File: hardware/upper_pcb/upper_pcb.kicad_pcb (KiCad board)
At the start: 2 copper layers, 54 x 54 mm, 12 parts, among them J5 FPC_6pin_0.5mm, SW4 Kailh_GM_8.0, SW5 Kailh_GM_8.0, SW6 Kailh_BlueDot_Side, SW7 Kailh_BlueDot_Side

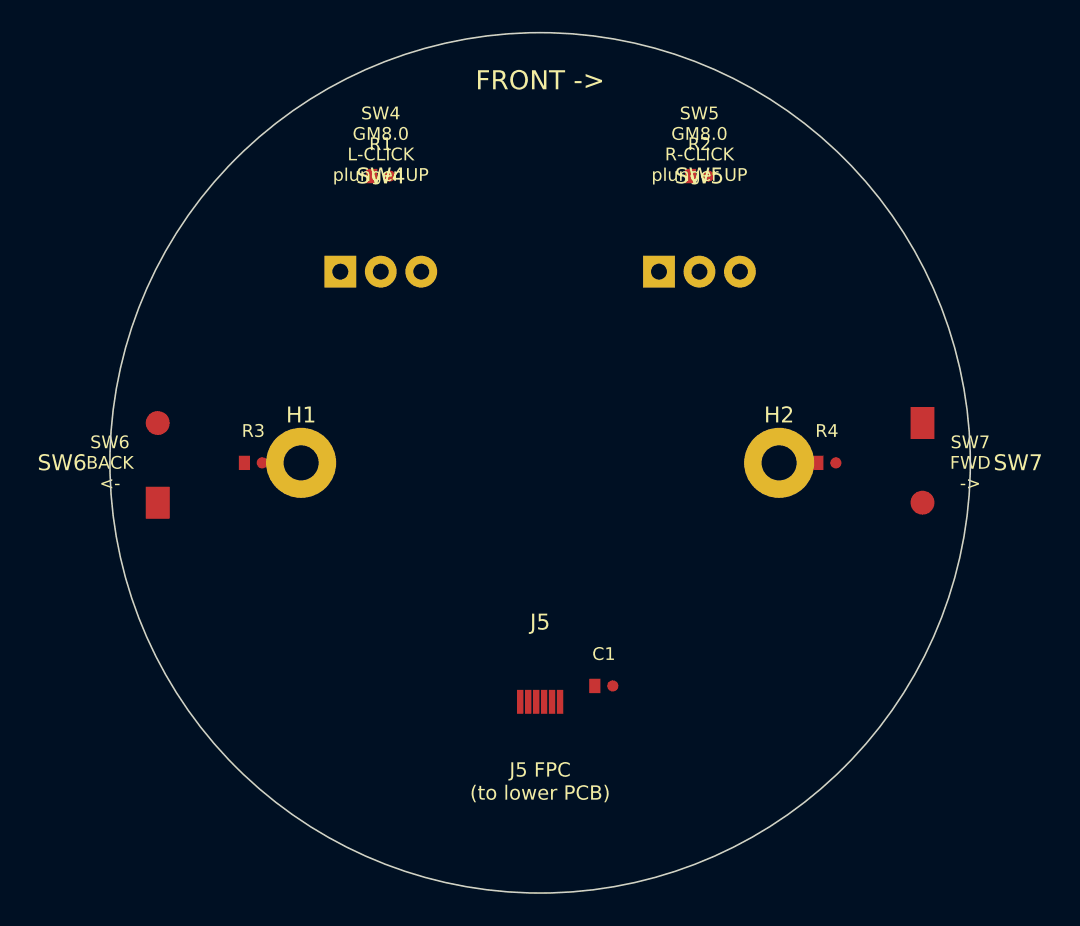
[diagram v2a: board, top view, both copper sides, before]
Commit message: feat: KiCad PCB files with full netlist and copper traces
lower_pcb.kicad_pcb (rev 2.4):
- All pads with correct net assignments
- 91 trace segments/vias covering all nets:
  3V3 rail, GND pour taps, VBUS, BAT_PLUS, SW_OUT (LDO)
  JOY_X/Y/SW from XIAO to Alps RKJXV pads
  BTN_L/R/BK/FW from XIAO to FPC J3 pins
  BT_SYNC from XIAO to SW_BT + R_PU_BT
  BAT_PLUS on B.Cu from J2 to SW1
- Via to B.Cu for J2 battery connector routing

upper_pcb.kicad_pcb (rev 1.6):
- All pads: SW4/SW5 GM8.0 THT, SW6/SW7 Blue Dot SMD, R1-R4, C1, J5 FPC on B.Cu
- 52 trace segments/vias:
  3V3 rail via from J5 B.Cu through to F.Cu R1-R4 pull-ups
  GND rail to all switch COM/GND pads and C1
  BTN_L/R via FPC->pull-up->switch signal pad for all 4 buttons

Open in KiCad 7, run DRC, fix any remaining unrouted connections with interactive router
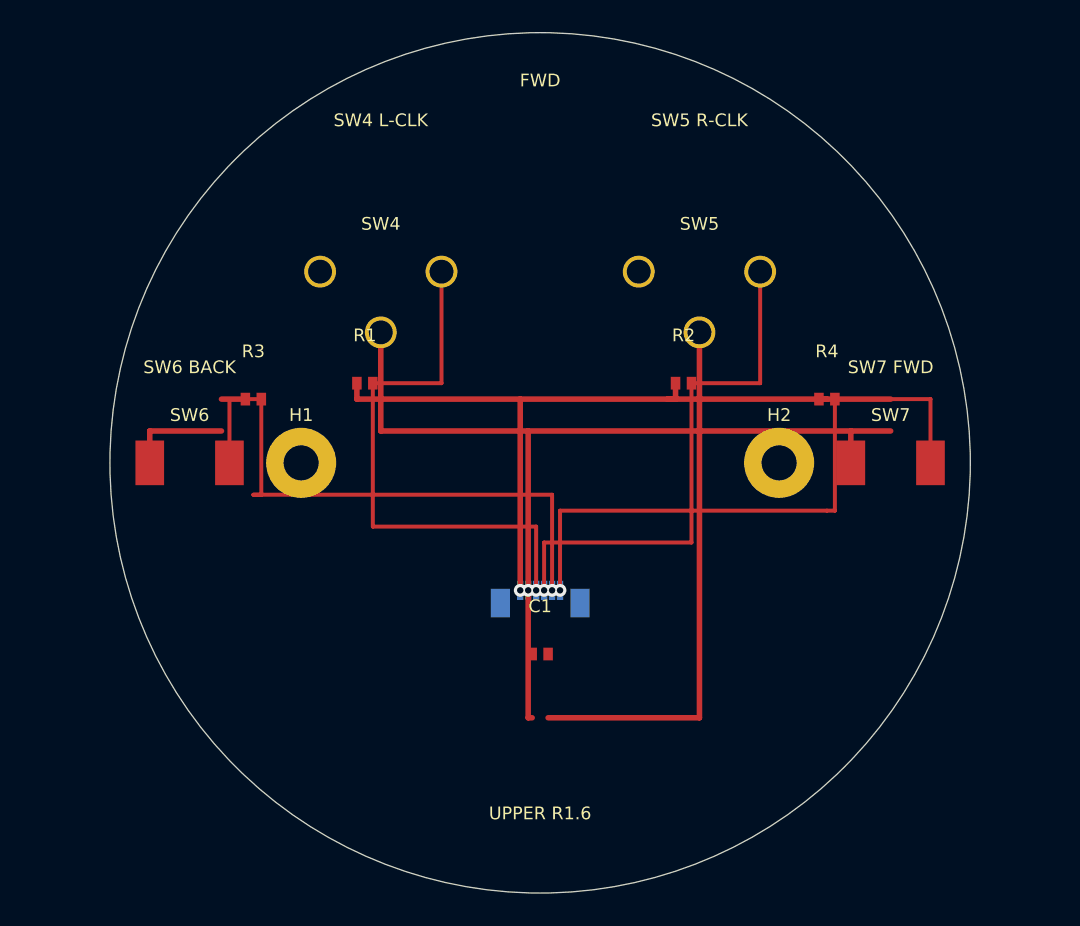
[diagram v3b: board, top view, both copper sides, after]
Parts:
- C1: value 100nF -> C-0402; footprint Capacitor_SMD:C_0402_1005Metric -> C1
- H1: value MountingHole_M2 -> M2-Mount; footprint MountingHole:MountingHole_2.2mm_M2_Pad -> H1
- H2: value MountingHole_M2 -> M2-Mount; footprint MountingHole:MountingHole_2.2mm_M2_Pad -> H2
- J5: value FPC_6pin_0.5mm -> FPC-6P-0.5mm; footprint Connector_FFC-FPC:Hirose_FH12-6S-0.5SH_1x06-1MP_P0.5mm_Horizontal -> J5; moved to B.Cu
- R1: value 10k -> R-0402; footprint Resistor_SMD:R_0402_1005Metric -> R1
- R2: value 10k -> R-0402; footprint Resistor_SMD:R_0402_1005Metric -> R2
- R3: value 10k -> R-0402; footprint Resistor_SMD:R_0402_1005Metric -> R3
- R4: value 10k -> R-0402; footprint Resistor_SMD:R_0402_1005Metric -> R4
- SW4: value Kailh_GM_8.0 -> Kailh-GM8.0; footprint Button_Switch_THT:SW_Push_SPDT_CherryMX_12.8x5.8mm -> SW4
- SW5: value Kailh_GM_8.0 -> Kailh-GM8.0; footprint Button_Switch_THT:SW_Push_SPDT_CherryMX_12.8x5.8mm -> SW5
- SW6: value Kailh_BlueDot_Side -> Kailh-BlueDot; footprint Button_Switch_SMD:SW_Push_Side_8.75mm -> SW6
- SW7: value Kailh_BlueDot_Side -> Kailh-BlueDot; footprint Button_Switch_SMD:SW_Push_Side_8.75mm -> SW7
- moved R1 13.0 mm to (89.0, 95.0)
- moved R2 13.0 mm to (109.0, 95.0)
- moved J5 7.00 mm to (100.0, 108.0)
- moved C1 4.47 mm to (100.0, 112.0)
- moved R3 4.00 mm to (82.0, 96.0)
- moved R4 4.00 mm to (118.0, 96.0)
- moved SW6 2.00 mm to (78.0, 100.0), turned to 0 degrees
- moved SW7 2.00 mm to (122.0, 100.0), turned to 0 degrees
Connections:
- net BTN_BACK renamed BTN_BK
- net BTN_FWD renamed BTN_FW
- H1 pad 1: (no net) -> GND
- H2 pad 1: (no net) -> GND
- J5 pad 3: BTN_LEFT -> BTN_L
- J5 pad 4: BTN_RIGHT -> BTN_R
- R1 pad 2: BTN_LEFT -> BTN_L
- R2 pad 2: BTN_RIGHT -> BTN_R
- SW4 pad 2: BTN_LEFT -> GND
- SW4 pad 3: (no net) -> BTN_L
- SW5 pad 2: BTN_RIGHT -> GND
- SW5 pad 3: (no net) -> BTN_R
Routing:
- net GND: track 0.00 -> 90.4 mm, vias 0 -> 1
- net 3V3: track 0.00 -> 58.2 mm, vias 0 -> 1
- net BTN_FW: track 0.00 -> 39.2 mm, vias 0 -> 1
- net BTN_BK: track 0.00 -> 37.2 mm, vias 0 -> 1
- net BTN_L: track 0.00 -> 34.6 mm, vias 0 -> 1
- net BTN_R: track 0.00 -> 33.6 mm, vias 0 -> 1
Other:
- board text added: "FWD"
- board text added: "J5 FPC-DN"
- board text added: "SW4 L-CLK"
- board text added: "SW5 R-CLK"
- board text added: "SW6 BACK"
- board text added: "SW7 FWD"
- board text added: "UPPER R1.6"
- board text removed: "FRONT ->"
- board text removed: "J5 FPC (to lower PCB)"
- board text removed: "SW4 GM8.0 L-CLICK plunger UP"
- board text removed: "SW5 GM8.0 R-CLICK plunger UP"
- board text removed: "SW6 BACK <-"
- board text removed: "SW7 FWD ->"
